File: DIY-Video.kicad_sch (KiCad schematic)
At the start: 8 parts, among them J1 VIDEO IO, J2 Host Address Bus, J3 Host Data Bus, J4 Host Control Bus, U61 74LS21, U66 74LS00, U67 74LS32, U8 74LS14

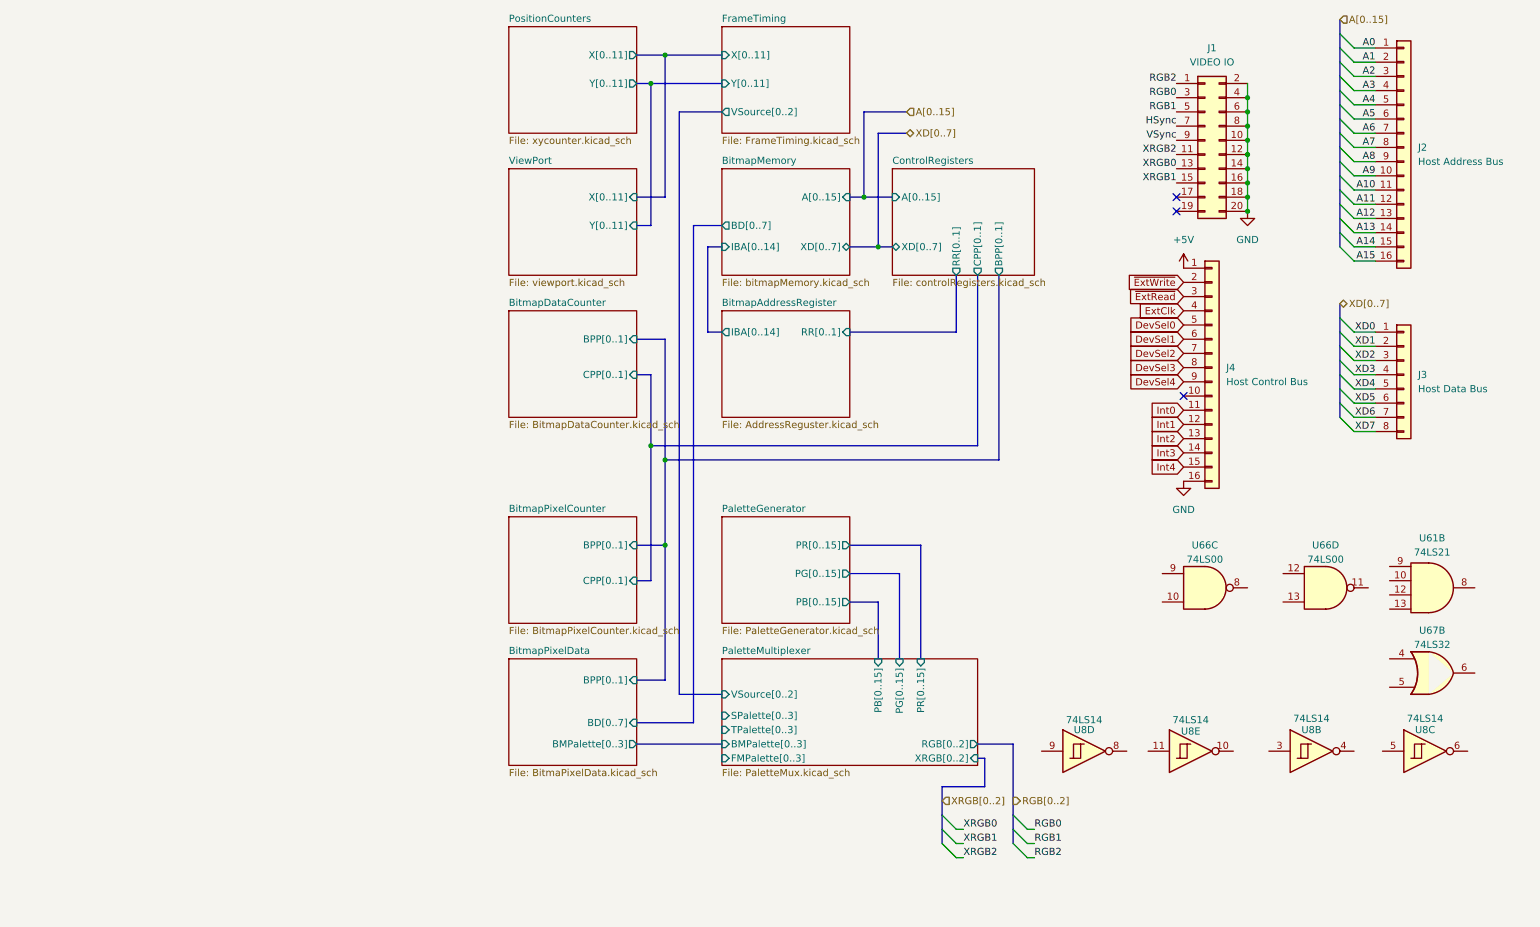
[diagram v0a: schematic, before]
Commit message: introduce PDF output from schematics
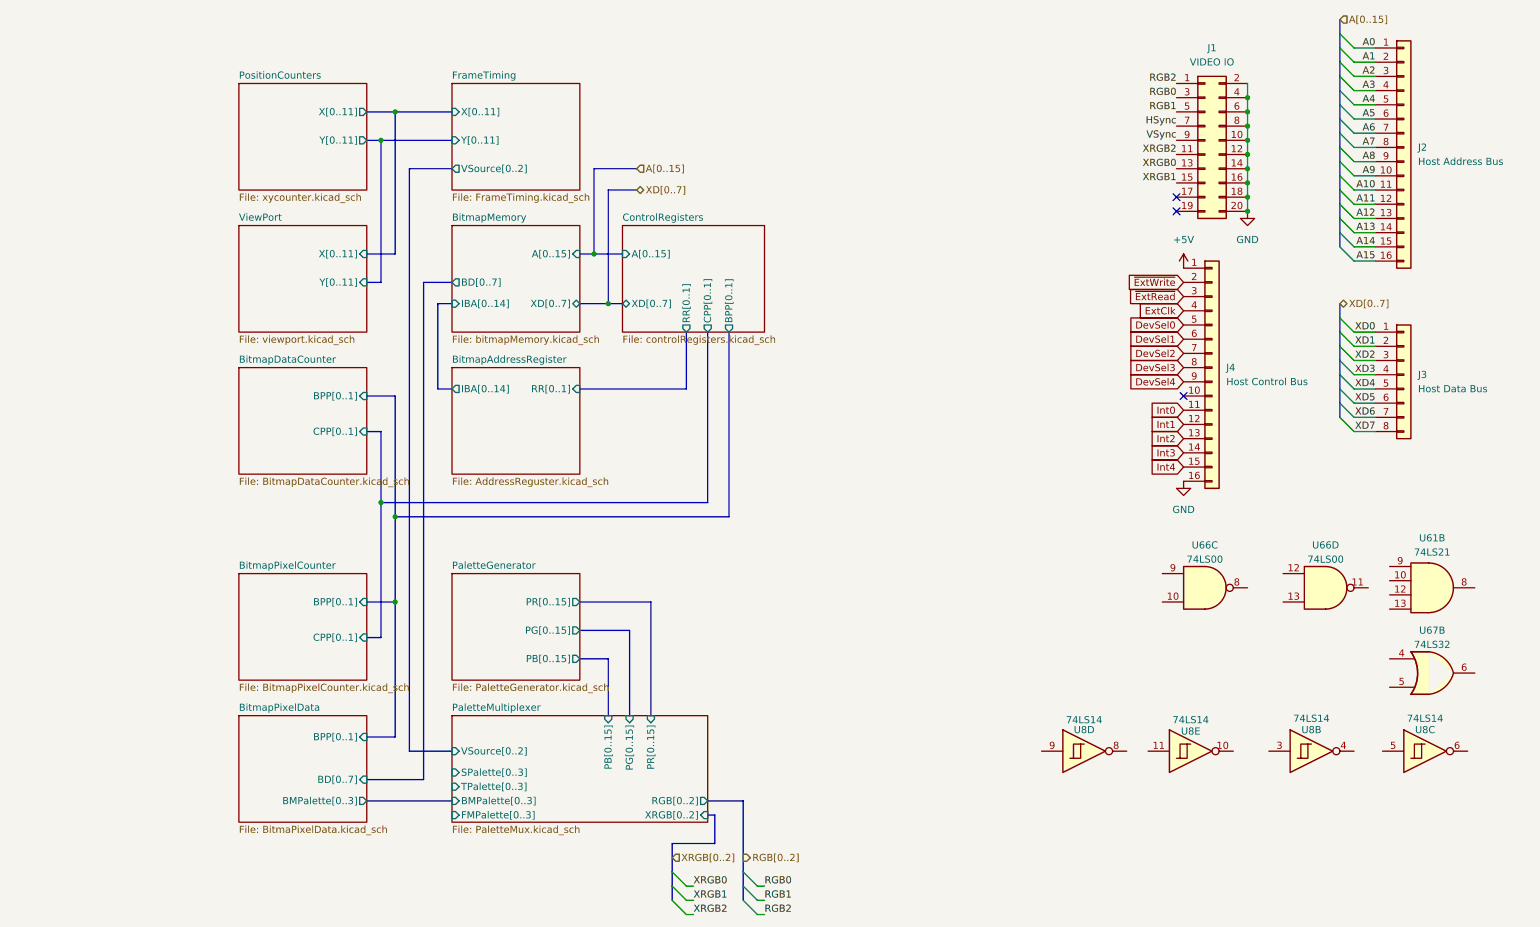
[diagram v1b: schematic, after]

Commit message: fix position counter Y reset logic
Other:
- added sheet DragonInterface (Interface0.kicad_sch)
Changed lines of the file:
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@@
+	)
+	(sheet
+		(at 16.51 25.4)
+		(size 22.86 19.05)
+		(exclude_from_sim no)
+		(in_bom yes)
+		(on_board yes)
+		(dnp no)
+		(fields_autoplaced yes)
+		(stroke
+			(width 0.1524)
+			(type solid)
+		)
+		(fill
+			(color 0 0 0 0.0000)
+		)
+		(property "Sheetname" "DragonInterface"
+			(at 16.51 24.6884 0)
+			(effects
+				(font
+					(size 1.27 1.27)
+				)
+				(justify left bottom)
+			)
+		)
+		(property "Sheetfile" "Interface0.kicad_sch"
+			(at 16.51 45.0346 0)
+			(effects
+				(font
+					(size 1.27 1.27)
+				)
+				(justify left top)
+			)
+		)
+		(instances
+			(project "DIY-Video"
+				(path "/6c4ef05c-ecf5-4bee-ae4e-d72f13738678"
+					(page "13")
+				)
+			)
+		)
 	)
 	(sheet

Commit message: isolate each schematic function for testing
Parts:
- removed U8: 74LS14, Package_SO:SO-14_3.9x8.65mm_P1.27mm, symbol 74xx:74LS14
- added U103: 74LS04, symbol 74xx:74LS04

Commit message: rework schematic isolation
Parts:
- removed U67: 74LS32, Package_SO:SO-14_3.9x8.65mm_P1.27mm, symbol 74xx:74LS32
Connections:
- no-connect marks 3 -> 7
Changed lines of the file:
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@@
+	)
+	(no_connect
+		(at 259.08 130.81)
 	)
 	(no_connect
@@
 	(no_connect
 		(at 224.79 45.72)
+	)
+	(no_connect
+		(at 259.08 115.57)
+	)
+	(no_connect
+		(at 237.49 115.57)
+	)
+	(no_connect
+		(at 278.13 115.57)
 	)
 	(no_connect
@@
 				)
 			)
-		)
-	)
-	(symbol
-		(lib_id "74xx:74LS32")
-		(at 270.51 130.81 0)
-		(unit 2)
-		(exclude_from_sim no)
-		(in_bom yes)
-		(on_board yes)
-		(dnp no)
-		(fields_autoplaced yes)
-		(property "Reference" "U67"
-			(at 270.51 123.19 0)
-			(effects
-				(font
-					(size 1.27 1.27)
-				)
-			)
-		)
-		(property "Value" "74LS32"
-			(at 270.51 125.73 0)
-			(effects
-				(font
-					(size 1.27 1.27)
-				)
-			)
-		)
-		(property "Footprint" "Package_SO:SO-14_3.9x8.65mm_P1.27mm"
-			(at 270.51 130.81 0)
-			(effects
-				(font
-					(size 1.27 1.27)
-				)
-				(hide yes)
-			)
-		)
-		(property "Datasheet" "http://www.ti.com/lit/gpn/sn74LS32"
-			(at 270.51 130.81 0)
-			(effects
-				(font
-					(size 1.27 1.27)
-				)
-				(hide yes)
-			)
-		)
-		(property "Description" "Quad 2-input OR"
-			(at 270.51 130.81 0)
-			(effects
-				(font
-					(size 1.27 1.27)
-				)
-				(hide yes)
-			)
-		)
-		(pin "3"
-		)
-		(pin "2"
-		)
-		(pin "1"
-		)
-		(pin "13"
-		)
-		(pin "9"
-		)
-		(pin "4"
-		)
-		(pin "12"
-		)
-		(pin "8"
-		)
-		(pin "6"
-		)
-		(pin "11"
-		)
-		(pin "14"
-		)
-		(pin "5"
-		)
-		(pin "7"
-		)
-		(pin "10"
-		)
-		(instances
-			(project "DIY-Video"
-				(path "/6c4ef05c-ecf5-4bee-ae4e-d72f13738678"
-					(reference "U67")
-					(unit 2)
-				)
-			)

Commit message: spin register out as separate board
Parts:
- U103: footprint (none) -> Package_SO:SOIC-14_3.9x8.7mm_P1.27mm
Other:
- added sheet ControlRegisterBankSelect (RegisterBank.kicad_sch)
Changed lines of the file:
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@@
 	(bus
 		(pts
-			(xy 120.65 55.88) (xy 120.65 40.64)
+			(xy 120.65 55.88) (xy 120.65 17.78)
 		)
 		(stroke
@@
 		)
 	)
-	(bus
-		(pts
-			(xy 123.19 44.45) (xy 128.27 44.45)
-		)
-		(stroke
-			(width 0)
-			(type default)
-		)
-	)
 	(wire
 		(pts
@@
 		)
 	)
-	(bus
-		(pts
-			(xy 120.65 40.64) (xy 128.27 40.64)
-		)
-		(stroke
-			(width 0)
-			(type default)
-		)
-	)
 	(wire
 		(pts
@@
 	(bus
 		(pts
-			(xy 123.19 64.77) (xy 123.19 44.45)
+			(xy 123.19 64.77) (xy 123.19 21.59)
 		)
 		(stroke
@@
 	(hierarchical_label "A[0..15]"
 		(shape input)
-		(at 128.27 40.64 0)
+		(at 120.65 17.78 0)
 		(effects
 			(font
@@
 	(hierarchical_label "XD[0..7]"
 		(shape bidirectional)
-		(at 128.27 44.45 0)
+		(at 123.19 21.59 0)
 		(effects
 			(font
@@
 			)
 		)
-		(property "Footprint" ""
+		(property "Footprint" "Package_SO:SOIC-14_3.9x8.7mm_P1.27mm"
 			(at 251.46 130.81 0)
 			(effects
@@
 				)
 			)
+		)
+	)
+	(sheet
+		(at 125.73 25.4)
+		(size 25.4 19.05)
+		(exclude_from_sim no)
+		(in_bom yes)
+		(on_board yes)
+		(dnp no)
+		(fields_autoplaced yes)
+		(stroke
+			(width 0.1524)
+			(type solid)
+		)
+		(fill
+			(color 0 0 0 0.0000)
+		)
+		(property "Sheetname" "ControlRegisterBankSelect"
+			(at 125.73 24.6884 0)
+			(effects
+				(font
+					(size 1.27 1.27)
+				)
+				(justify left bottom)
+			)
+		)
+		(property "Sheetfile" "RegisterBank.kicad_sch"
+			(at 125.73 45.0346 0)
+			(effects
+				(font
+					(size 1.27 1.27)
+				)
+				(justify left top)
+			)
+		)
+		(instances
+			(project "DIY-Video"
+				(path "/6c4ef05c-ecf5-4bee-ae4e-d72f13738678"
+					(page "14")
+				)
+			)

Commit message: tighten layout for final sizing
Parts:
- removed J2: Host Address Bus, Connector_PinHeader_2.54mm:PinHeader_1x16_P2.54mm_Vertical, symbol Connector_Generic:Conn_01x16
- removed J3: Host Data Bus, Connector_PinHeader_2.54mm:PinHeader_1x08_P2.54mm_Vertical, symbol Connector_Generic:Conn_01x08
- removed J4: Host Control Bus, Connector_PinHeader_2.54mm:PinHeader_1x16_P2.54mm_Vertical, symbol Connector_Generic:Conn_01x16
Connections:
- no-connect marks 7 -> 6
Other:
- added sheet RegisterInterface (RegisterIO.kicad_sch)
